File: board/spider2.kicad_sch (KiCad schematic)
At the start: 100 parts, among them J1 NRJ6HH-1, J10 PJ-320A, J11 PJ358, J12 PJ358, J13 PJ358, J14 PJ358, J15 PJ358, J16 PJ358, J19 PJ358, J2 NRJ6HH-1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

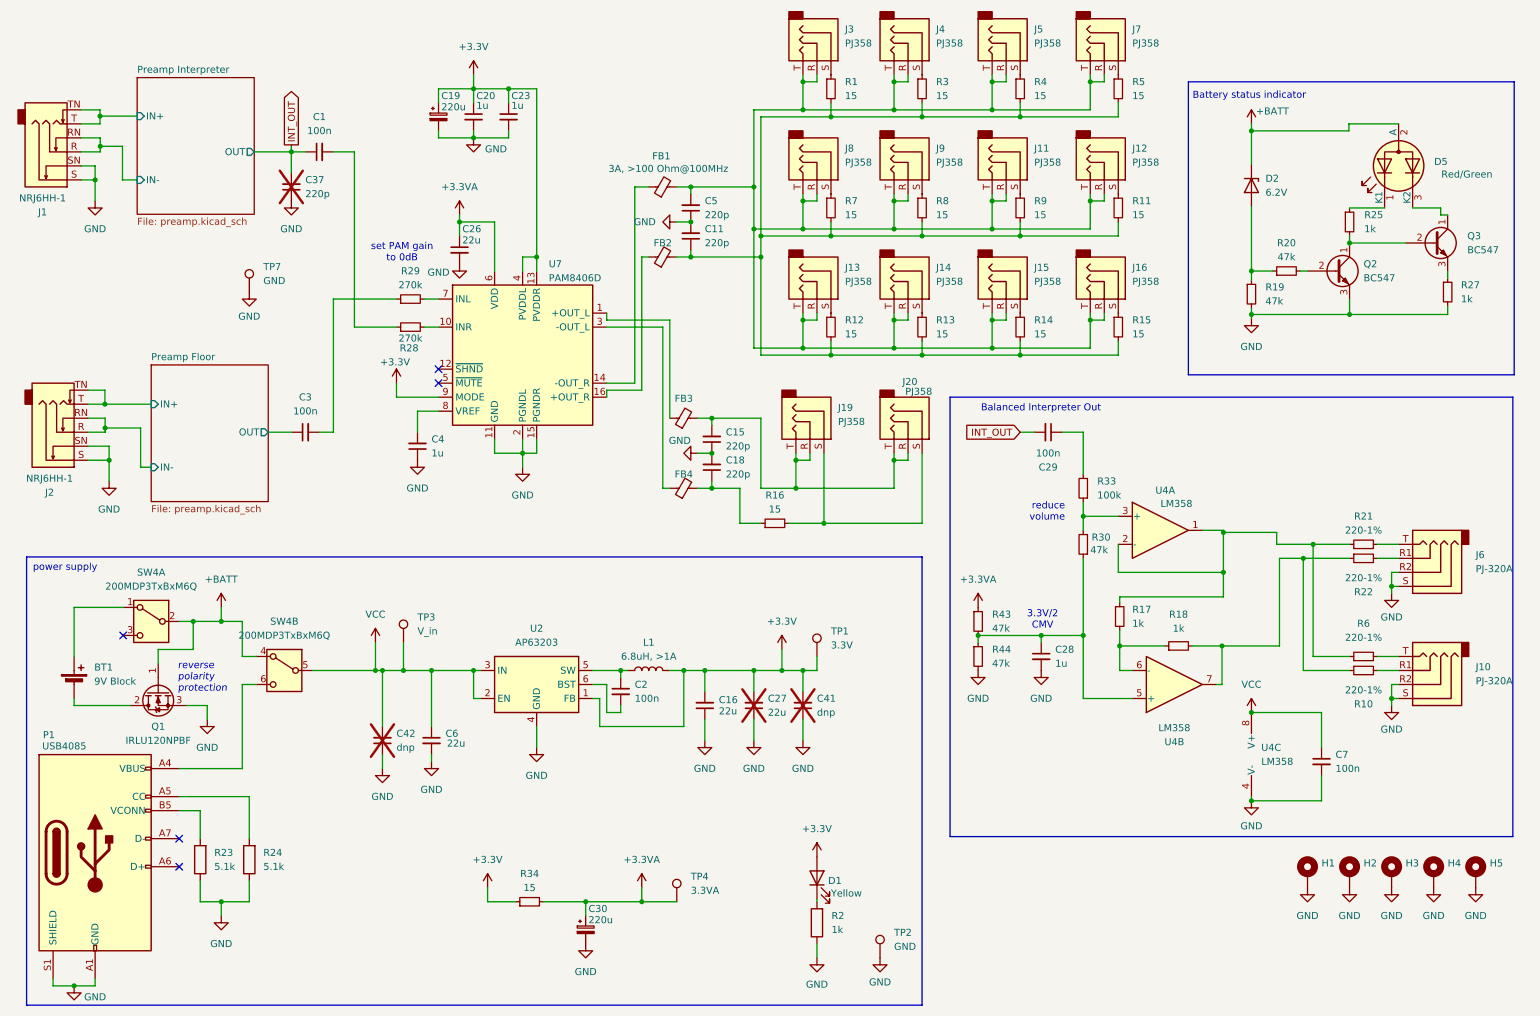
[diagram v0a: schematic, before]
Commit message: redesigned MAX section with shorter traces, analog GND plane,...
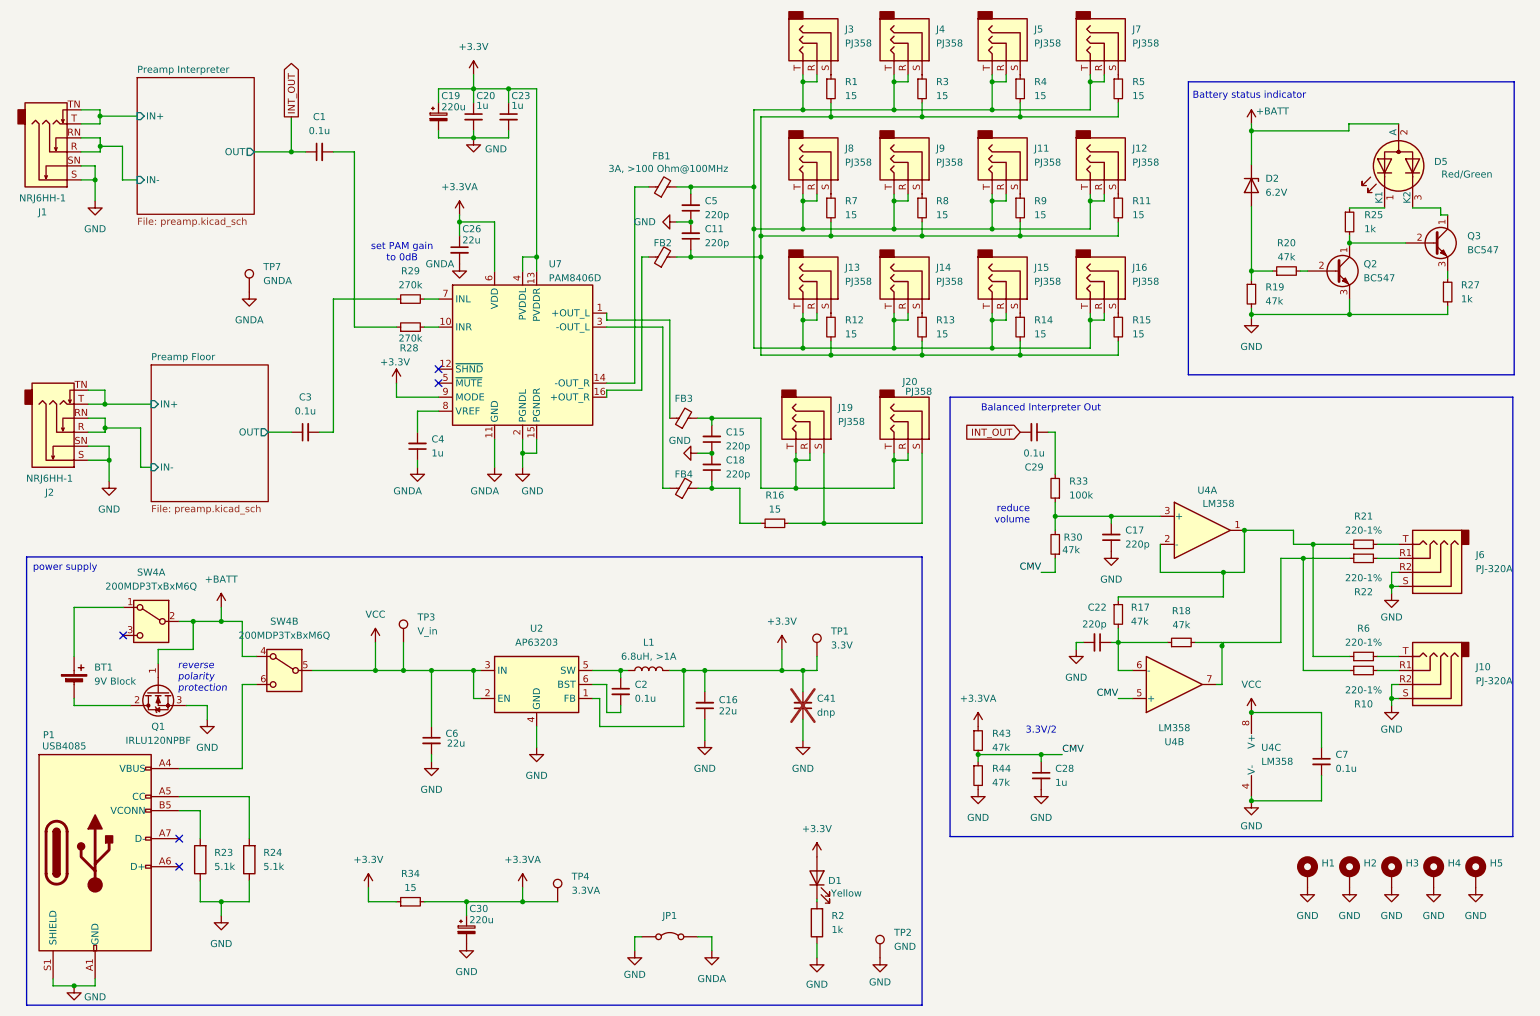
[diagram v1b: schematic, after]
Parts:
- removed C27: 22u, Capacitor_SMD:C_1206_3216Metric_Pad1.33x1.80mm_HandSolder, symbol Device:C_Small
- removed C37: 220p, Capacitor_THT:C_Disc_D3.0mm_W2.0mm_P2.50mm, symbol Device:C_Small
- removed C42: dnp, Capacitor_THT:C_Disc_D4.3mm_W1.9mm_P5.00mm, symbol Device:C_Small
- added C17, C22: 220p, Capacitor_THT:C_Disc_D3.0mm_W2.0mm_P2.50mm, symbol Device:C_Small
- added JP1: ~, Jumper:SolderJumper-2_P1.3mm_Bridged2Bar_RoundedPad1.0x1.5mm, symbol Jumper:Jumper_2_Bridged
- C1, C2, C29, C3, C7: value 100n -> 0.1u
- C30: now in the parts list
- R10, R21, R22, R6: footprint Resistor_THT:R_Axial_DIN0207_L6.3mm_D2.5mm_P10.16mm_Horizontal -> Resistor_THT:R_Axial_DIN0204_L3.6mm_D1.6mm_P5.08mm_Horizontal
- R17, R18: value 1k -> 47k
- TP7: value GND -> GNDA
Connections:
- net GND: now also C17.1, C22.2, JP1.1 (A); no longer C26.2, C4.1, TP7.1, U7.11 (GND)
- net CMV: now reaches C28.1, R30.1, R43.2, R44.1, U4.5 (+)
- net at R17.2, R18.1, U4.6 (-): now also C22.1
- net at R30.2, R33.1, U4.3 (+): now also C17.2
- new net GNDA: C26.2, C4.1, JP1.2 (B), TP7.1, U7.11 (GND)
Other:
- note added: "3.3V/2"
- note removed: "3.3V/2 CMV"
- moved on the sheet: C28, C29, C30, R18, R30, R33, R34, R43, R44, TP4, U4A

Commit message: revert separating ground planes
maybe it leads to more issues than it solves
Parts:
- removed JP1: ~, Jumper:SolderJumper-2_P1.3mm_Bridged2Bar_RoundedPad1.0x1.5mm, symbol Jumper:Jumper_2_Bridged
- C2: Note (none) -> ≥20V
- C6, C7: Note (none) -> ≥16V
- FB1: value 3A, >100 Ohm@100MHz -> 3A/≥100 Ohm
- L1: value 6.8uH, >1A -> 6.8uH; Note (none) -> ≥1A, <100mOhm
- R10, R21, R22, R6: value 220-1% -> 220; Note (none) -> 1%
- TP7: value GNDA -> GND
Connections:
- net GNDA is gone; now on net GND: C26.2, C4.1, TP7.1, U7.11 (GND)

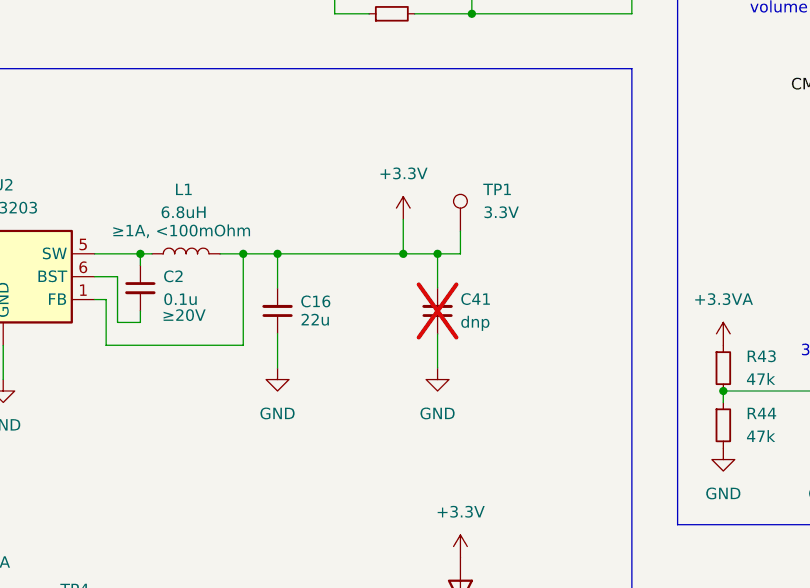
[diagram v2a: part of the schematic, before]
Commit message: clearer separation of sections, test marks,...
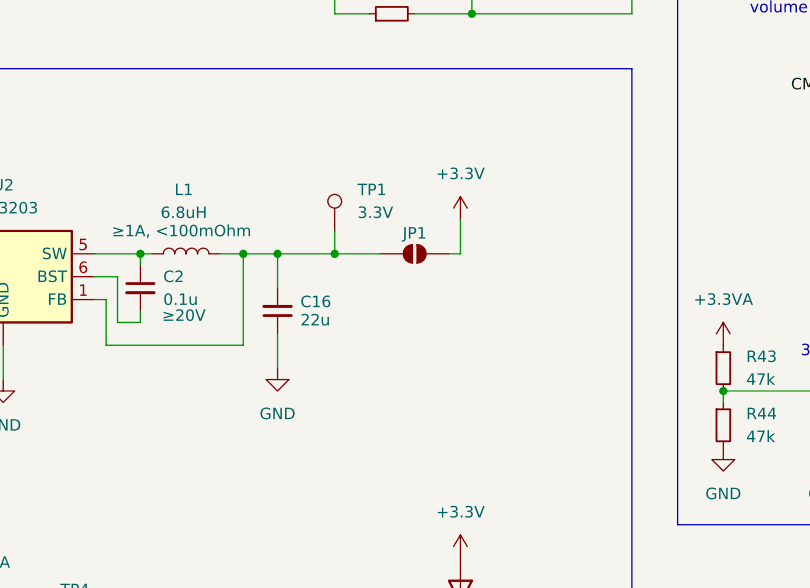
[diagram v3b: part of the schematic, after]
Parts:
- removed C41: dnp, Capacitor_THT:C_Disc_D4.3mm_W1.9mm_P5.00mm, symbol Device:C_Small
- added JP1: ~, Jumper:SolderJumper-2_P1.3mm_Open_RoundedPad1.0x1.5mm, symbol Jumper:SolderJumper_2_Open
- FB2, FB3, FB4: value 3A, >100 Ohm@100MHz -> 3A/≥100 Ohm
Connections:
- net +3.3V: now also JP1.2 (B); no longer C16.2, L1.2, TP1.1, U2.1 (FB)
- new net: C16.2, JP1.1 (A), L1.2, TP1.1, U2.1 (FB)
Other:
- moved on the sheet: TP1

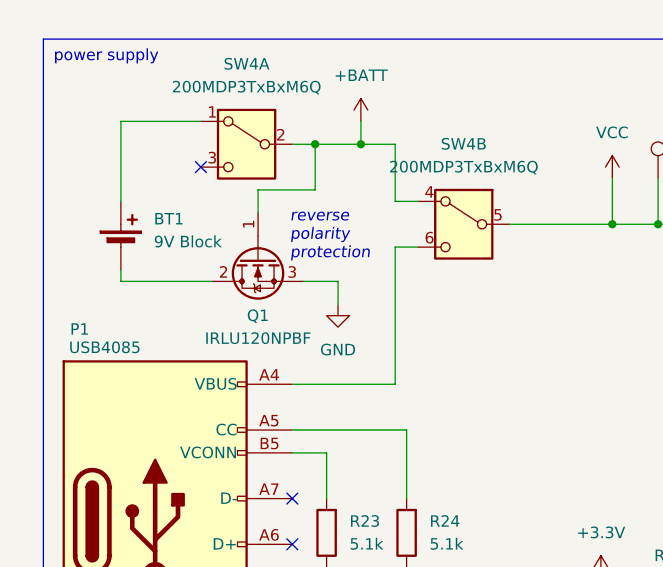
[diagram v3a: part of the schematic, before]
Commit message: some cleanups, cheaper MOSFET,  datasheet links,
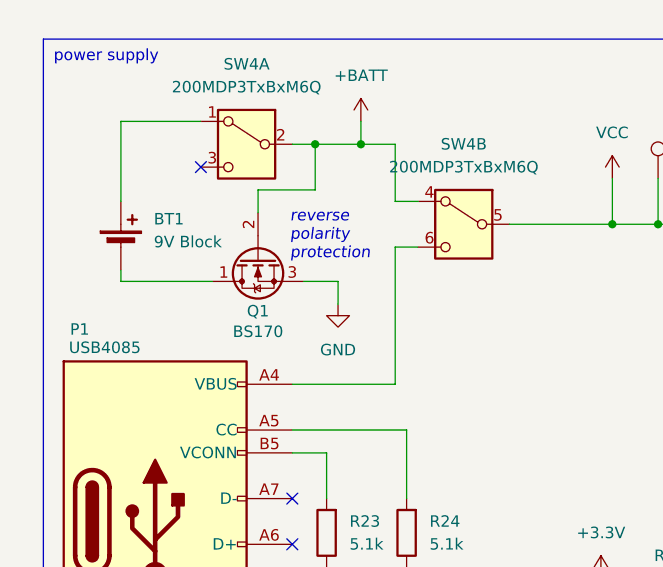
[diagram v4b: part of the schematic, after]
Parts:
- removed Q1: IRLU120NPBF, Package_TO_SOT_THT:TO-251-3_Vertical, symbol Device:Q_NMOS_GDS
- added Q1: BS170, Package_TO_SOT_THT:TO-92_Inline_Wide, symbol Transistor_FET:BS170
- J1, J2: footprint Connector_Audio:Jack_6.35mm_Neutrik_NRJ6HH_Horizontal -> Connector_Audio:Jack_6.35mm_Neutrik_NRJ6HH-1_Horizontal
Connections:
- net +BATT: now also Q1.2 (G)
- net GND: now also Q1.3 (S)
- net at BT1.2 (-): now also Q1.1 (D)
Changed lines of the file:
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@@
 	)
 	(symbol
+		(lib_id "Transistor_FET:BS170")
+		(at 38.1 138.43 90)
+		(mirror x)
+		(unit 1)
+		(exclude_from_sim no)
+		(in_bom yes)
+		(on_board yes)
+		(dnp no)
+		(property "Reference" "Q1"
+			(at 38.1 144.272 90)
+			(effects
+				(font
+					(size 1.27 1.27)
+				)
+			)
+		)
+		(property "Value" "BS170"
+			(at 38.1 146.558 90)
+			(effects
+				(font
+					(size 1.27 1.27)
+				)
+			)
+		)
+		(property "Footprint" "Package_TO_SOT_THT:TO-92_Inline_Wide"
+			(at 40.005 143.51 0)
+			(effects
+				(font
+					(size 1.27 1.27)
+					(italic yes)
+				)
+				(justify left)
+				(hide yes)
+			)
+		)
+		(property "Datasheet" "https://www.onsemi.com/pub/Collateral/BS170-D.PDF"
+			(at 41.91 143.51 0)
+			(effects
+				(font
+					(size 1.27 1.27)
+				)
+				(justify left)
+				(hide yes)
+			)
+		)
+		(property "Description" "0.5A Id, 60V Vds, N-Channel MOSFET, TO-92"
+			(at 38.1 138.43 0)
+			(effects
+				(font
+					(size 1.27 1.27)
+				)
+				(hide yes)
+			)
+		)
+		(property "Note" "wide leads (D)"
+			(at 38.1 138.43 0)
+			(effects
+				(font
+					(size 1.27 1.27)
+				)
+				(hide yes)
+			)
+		)
+		(pin "3"
+		)
+		(pin "2"
+		)
+		(pin "1"
+		)
+		(instances
+			(project "spider2"
+				(path "/31073f88-a990-4ecc-8ab9-bb6b56c98e1e"
+					(reference "Q1")
+					(unit 1)
+				)
+			)
+		)
+	)
+	(symbol
 		(lib_id "Device:LED")
 		(at 157.48 172.212 90)
@@
 			)
 		)
-		(property "Datasheet" "~"
+		(property "Datasheet" "https://eu.mouser.com/datasheet/2/216/WP59EGW-CA-54724.pdf"
 			(at 262.89 44.45 0)
 			(effects
@@
 			)
 		)
+		(property "Note" ""
+			(at 262.89 43.18 0)
+			(effects
+				(font
+					(size 1.27 1.27)
+				)
+			)
+		)
 		(pin "2"
 		)
@@
 			)
 		)
-		(property "Datasheet" "http://www.ti.com/lit/ds/symlink/ne5532.pdf"
+		(property "Datasheet" "https://www.diodes.com/assets/Datasheets/LM358.pdf"
 			(at 222.25 137.16 0)
 			(effects
@@
 			)
 		)
+		(property "Note" ""
+			(at 222.25 137.16 0)
+			(effects
+				(font
+					(size 1.27 1.27)
+				)
+			)
+		)
 		(pin "6"
 		)
@@
 			)
 		)
-		(property "Footprint" "Connector_Audio:Jack_6.35mm_Neutrik_NRJ6HH_Horizontal"
+		(property "Footprint" "Connector_Audio:Jack_6.35mm_Neutrik_NRJ6HH-1_Horizontal"
 			(at 20.32 91.44 0)
 			(effects
@@
 			)
 		)
+		(property "Note" ""
+			(at 20.32 91.44 0)
+			(effects
+				(font
+					(size 1.27 1.27)
+				)
+			)
+		)
 		(pin "S"
 		)
@@
 	)
 	(symbol
-		(lib_id "Device:Q_NMOS_GDS")
-		(at 38.1 138.43 90)
-		(mirror x)
-		(unit 1)
-		(exclude_from_sim no)
-		(in_bom yes)
-		(on_board yes)
-		(dnp no)
-		(property "Reference" "Q1"
-			(at 38.1 144.78 90)
-			(effects
-				(font
-					(size 1.27 1.27)
-				)
-			)
-		)
-		(property "Value" "IRLU120NPBF"
-			(at 38.1 147.32 90)
-			(effects
-				(font
-					(size 1.27 1.27)
-				)
-			)
-		)
-		(property "Footprint" "Package_TO_SOT_THT:TO-251-3_Vertical"
-			(at 35.56 143.51 0)
-			(effects
-				(font
-					(size 1.27 1.27)
-				)
-				(hide yes)
-			)
-		)
-		(property "Datasheet" "https://www.tme.eu/Document/0cc9448b759d8f4845600d6775144bd3/AOI4286.pdf"
-			(at 38.1 138.43 0)
-			(effects
-				(font
-					(size 1.27 1.27)
-				)
-				(hide yes)
-			)
-		)
-		(property "Description" "N-MOSFET transistor, gate/drain/source"
-			(at 38.1 138.43 0)
-			(effects
-				(font
-					(size 1.27 1.27)
-				)
-				(hide yes)
-			)
-		)
-		(property "Sim.Device" ""
-			(at 38.1 138.43 0)
-			(effects
-				(font
-					(size 1.27 1.27)
-				)
-				(hide yes)
-			)
-		)
-		(property "Sim.Pins" ""
-			(at 38.1 138.43 0)
-			(effects
-				(font
-					(size 1.27 1.27)
-				)
-				(hide yes)
-			)
-		)
-		(property "Sim.Type" ""
-			(at 38.1 138.43 0)
-			(effects
-				(font
-					(size 1.27 1.27)
-				)
-				(hide yes)
-			)
-		)
-		(pin "3"
-		)
-		(pin "2"
-		)
-		(pin "1"
-		)
-		(instances
-			(project "spider2"
-				(path "/31073f88-a990-4ecc-8ab9-bb6b56c98e1e"
-					(reference "Q1")
-					(unit 1)
-				)
-			)
-		)
-	)
-	(symbol
 		(lib_id "Connector_Audio:AudioJack3")
 		(at 173.99 21.59 270)
@@
 			)
 		)
-		(property "Datasheet" "https://www.onsemi.com/pub/Collateral/BC550-D.pdf"
+		(property "Datasheet" "https://diotec.com/request/datasheet/bc546.pdf"
 			(at 269.24 57.15 0)
 			(effects
@@
 			)
 		)
+		(property "Note" ""
+			(at 269.24 57.15 0)
+			(effects
+				(font
+					(size 1.27 1.27)
+				)
+			)
+		)
 		(pin "2"
 		)
@@
 			)
 		)
-		(property "Datasheet" "https://www.onsemi.com/pub/Collateral/BC550-D.pdf"
+		(property "Datasheet" "https://diotec.com/request/datasheet/bc546.pdf"
 			(at 251.46 62.23 0)
 			(effects
@@
 			)
 		)
+		(property "Note" ""
+			(at 251.46 62.23 0)
+			(effects
+				(font
+					(size 1.27 1.27)
+				)
+			)
+		)
 		(pin "2"
 		)
@@
 			)
 		)
-		(property "Datasheet" "http://www.ti.com/lit/ds/symlink/ne5532.pdf"
+		(property "Datasheet" "https://www.diodes.com/assets/Datasheets/LM358.pdf"
 			(at 227.33 109.22 0)
 			(effects
@@
 			)
 		)
+		(property "Note" ""
+			(at 227.33 109.22 0)
+			(effects
+				(font
+					(size 1.27 1.27)
+				)
+			)
+		)
 		(pin "6"
 		)
@@
 			)
 		)
-		(property "Datasheet" "http://www.ti.com/lit/ds/symlink/ne5532.pdf"
+		(property "Datasheet" "https://www.diodes.com/assets/Datasheets/LM358.pdf"
 			(at 238.76 149.86 0)
 			(effects
@@
 			)
 		)
+		(property "Note" ""
+			(at 238.76 149.86 0)
+			(effects
+				(font
+					(size 1.27 1.27)
+				)
+			)
+		)
 		(pin "6"
 		)
@@
 			)
 		)
-		(property "Datasheet" "https://www.usb.org/sites/default/files/documents/usb_type-c.zip"
+		(property "Datasheet" "https://www.mouser.de/datasheet/2/837/GCT_usb4085-3240028.pdf"
 			(at 30.48 167.64 0)
 			(effects
@@
 			)
 		)
+		(property "Note" ""
+			(at 26.67 167.64 0)
+			(effects
+				(font
+					(size 1.27 1.27)
+				)
+			)
+		)
 		(pin "B12"
 		)
@@
 			)
 		)
-		(property "Footprint" "Connector_Audio:Jack_6.35mm_Neutrik_NRJ6HH_Horizontal"
+		(property "Footprint" "Connector_Audio:Jack_6.35mm_Neutrik_NRJ6HH-1_Horizontal"
 			(at 19.05 40.64 0)
 			(effects
@@
 			)
 		)
-		(property "Datasheet" "https://www.neutrik.com/en/product/nrj6hh"
+		(property "Datasheet" "https://www.neutrik.com/media/9131/download/st-nrj6hh-1.PDF?v=2"
 			(at 19.05 40.64 0)
 			(effects
@@
 			)
 		)
+		(property "Note" ""
+			(at 19.05 40.64 0)
+			(effects
+				(font
+					(size 1.27 1.27)
+				)
+			)
+		)
